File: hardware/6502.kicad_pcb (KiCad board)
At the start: 2 copper layers, 149.9 x 99.1 mm, 80 parts, among them J1 JMP, J10 JMP, J11 Conn_01x04_Male, J12 Conn_01x08_Male, J13 Conn_01x08_Male, J14 Conn_01x06_Male, J15 Conn_01x08_Male, J16 Conn_01x16_Male, J2 Conn_01x16_Male, J3 CA, J4 CB, J5 W27c512?, J6 DB15_Female_HighDensity, J7 Conn_01x12_Male, J8 Barrel_Jack_MountingPin, J9 USB_B_Micro, SW1 SW_Push, U1 74HC00, U10 74HC245, U11 74HC245, U12 PMS171B-SOP16_150mil, U13 74HC245, U14 74HC04, U15 MIC5504-3.3YM5, U16 62256, U17 74LS00, U18 w27C512, U19 74LS161, U2 R6502, U20 74LS165, U3 R6522, U4 74HC273, U5 SST39SF010, U6 74LS161, U7 74LS161, U8 74LS32, U9 74HC245, Y1 16Mhz

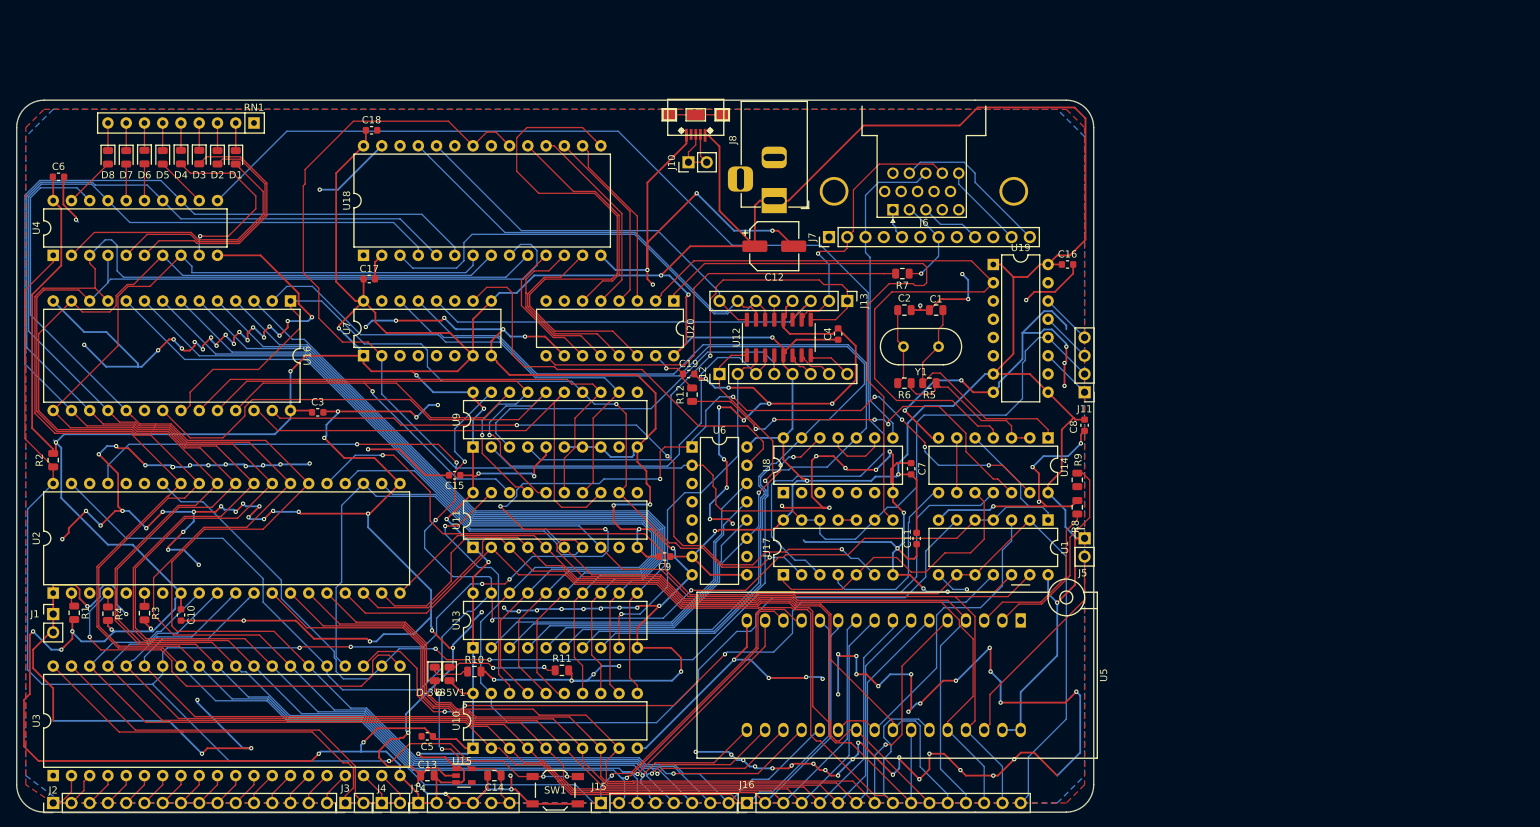
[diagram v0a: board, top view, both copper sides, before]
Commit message: PCB Silkscreen annotations added
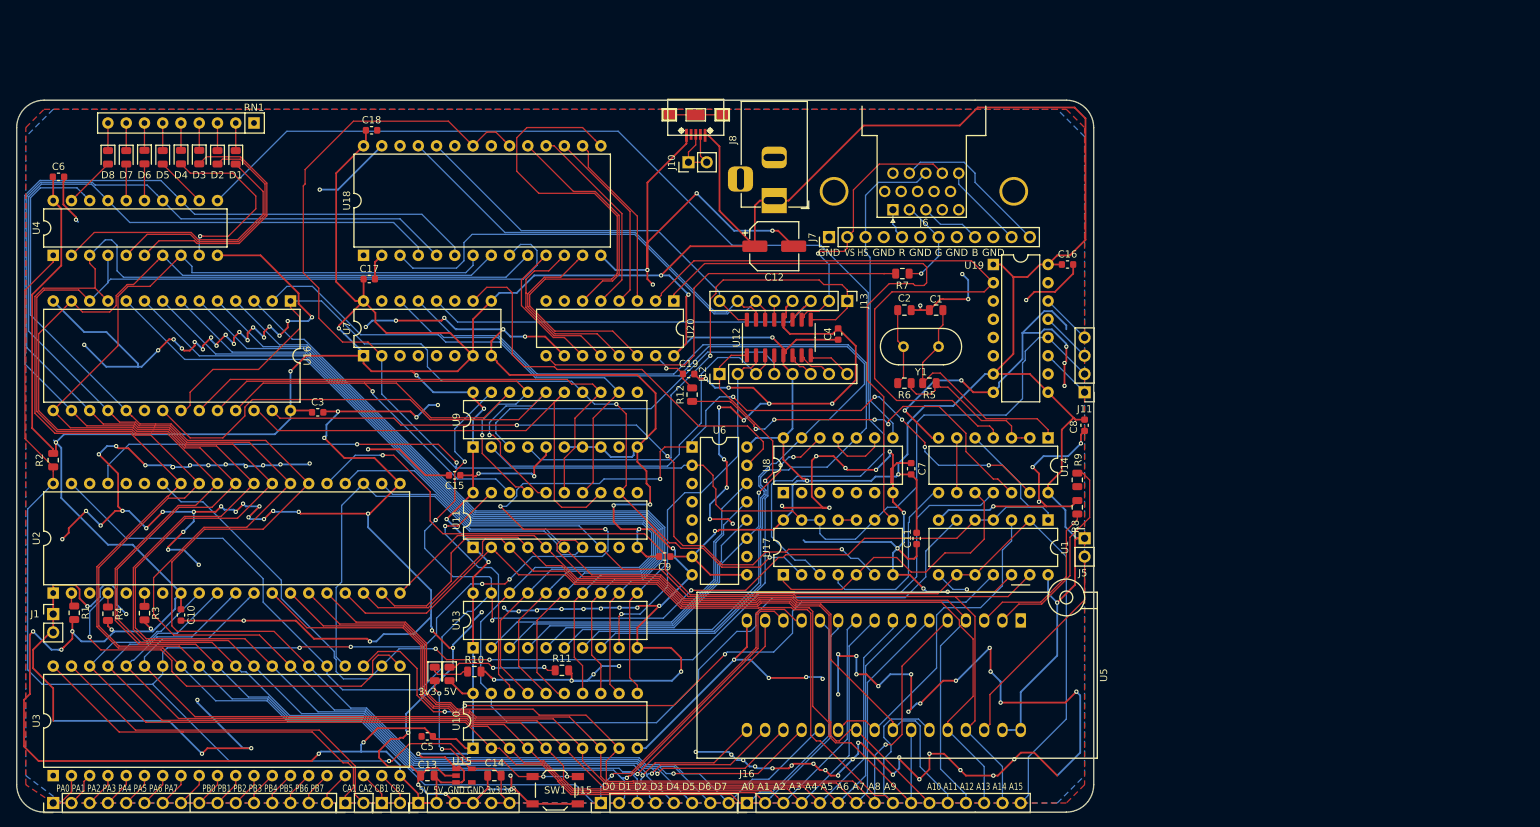
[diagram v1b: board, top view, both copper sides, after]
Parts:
- renumbered D-3v3 to 3v3, D-5V1 to 5V
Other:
- board text added: "5V 5V GND GND 3v3 3v3"
- board text added: "A0 A1 A2 A3 A4 A5 A6 A7 A8 A9"
- board text added: "A10 A11 A12 A13 A14 A15"
- board text added: "B"
- board text added: "CA1 CA2 CB1 CB2"
- board text added: "D0 D1 D2 D3 D4 D5 D6 D7"
- board text added: "G"
- board text added: "GND"
- board text added: "PA0 PA1 PA2 PA3 PA4 PA5 PA6 PA7"
- board text added: "PB0 PB1 PB2 PB3 PB4 PB5 PB6 PB7"
- board text added: "R"
- board text added: "VS HS"

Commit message: Wireless nRF24L01+ bootloader added! No more Padauk PMS171b!
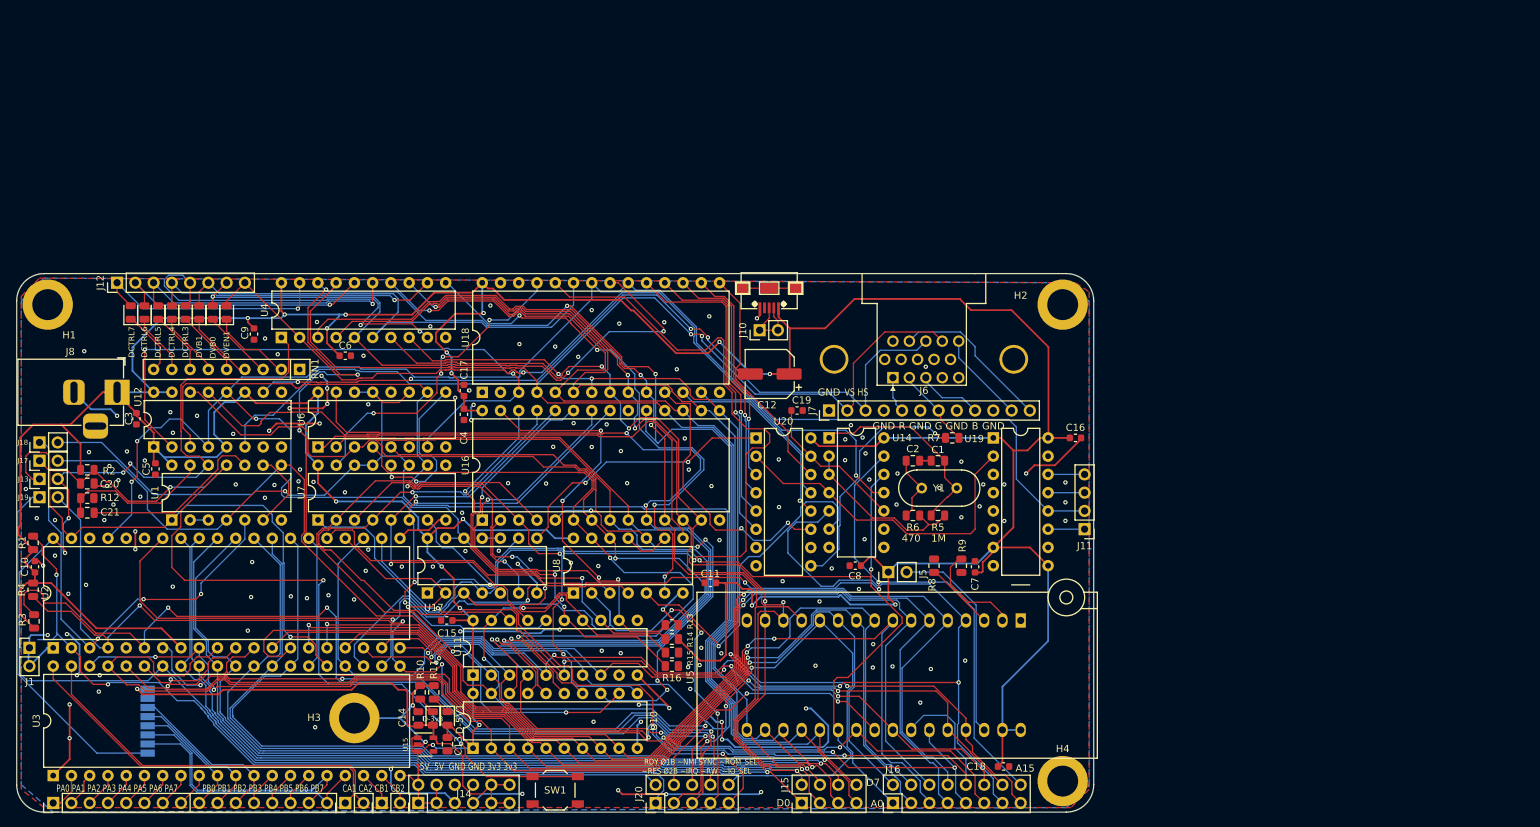
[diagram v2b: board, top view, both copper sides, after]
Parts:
- removed D1, D2, D3, D4, D5, D6, D7, D8: RED, LED_SMD:LED_0805_2012Metric
- removed U13: 74HC245, Package_DIP:DIP-20_W7.62mm
- added C20: 1uF, Capacitor_SMD:C_0805_2012Metric, F.Cu at (22.5, 120.7)
- added C21: 1uF, Capacitor_SMD:C_0805_2012Metric, F.Cu at (22.5, 124.7)
- added DCTRL3: RED, LED_SMD:LED_0805_2012Metric, F.Cu at (36.2, 96.9)
- added DCTRL4: RED, LED_SMD:LED_0805_2012Metric, F.Cu at (34.3, 96.9)
- added DCTRL5: RED, LED_SMD:LED_0805_2012Metric, F.Cu at (32.4, 96.9)
- added DCTRL6: RED, LED_SMD:LED_0805_2012Metric, F.Cu at (30.5, 96.9)
- added DCTRL7: RED, LED_SMD:LED_0805_2012Metric, F.Cu at (28.6, 96.9)
- added DVB0: RED, LED_SMD:LED_0805_2012Metric, F.Cu at (40.0, 96.9)
- added DVB1: RED, LED_SMD:LED_0805_2012Metric, F.Cu at (38.1, 96.9)
- added DVEN1: RED, LED_SMD:LED_0805_2012Metric, F.Cu at (41.9, 96.9)
- added H1: MountingHole_Pad, MountingHole:MountingHole_4.3mm_M4_ISO14580_Pad, F.Cu at (17.0, 95.8)
- added H2: MountingHole_Pad, MountingHole:MountingHole_4.3mm_M4_ISO14580_Pad, F.Cu at (158.2, 95.8)
- added H3: MountingHole_Pad, MountingHole:MountingHole_4.3mm_M4_ISO14580_Pad, F.Cu at (59.7, 153.3)
- added H4: MountingHole_Pad, MountingHole:MountingHole_4.3mm_M4_ISO14580_Pad, F.Cu at (158.2, 162.1)
- added J17: JMP, Connector_PinHeader_2.54mm:PinHeader_1x02_P2.54mm_Vertical, F.Cu at (15.9, 117.5)
- added J18: JMP, Connector_PinHeader_2.54mm:PinHeader_1x02_P2.54mm_Vertical, F.Cu at (15.9, 114.9)
- added J19: JMP, Connector_PinHeader_2.54mm:PinHeader_1x02_P2.54mm_Vertical, F.Cu at (15.9, 122.6)
- added J20: Interface, Connector_PinHeader_2.54mm:PinHeader_2x05_P2.54mm_Vertical, F.Cu at (101.6, 165.1)
- added R13: 2k2, Resistor_SMD:R_0805_2012Metric, F.Cu at (103.9, 140.3)
- added R14: 2k2, Resistor_SMD:R_0805_2012Metric, F.Cu at (103.9, 142.3)
- added R15: 2k2, Resistor_SMD:R_0805_2012Metric, F.Cu at (103.9, 144.2)
- added R16: 2k2, Resistor_SMD:R_0805_2012Metric, F.Cu at (103.9, 146.1)
- J12: value Conn_01x08_Male -> Control_bus
- J13: value Conn_01x08_Male -> EzRST; footprint Connector_PinHeader_2.54mm:PinHeader_1x08_P2.54mm_Vertical -> Connector_PinHeader_2.54mm:PinHeader_1x02_P2.54mm_Vertical
- J14: value Conn_01x06_Male -> Power; footprint Connector_PinHeader_2.54mm:PinHeader_1x06_P2.54mm_Vertical -> Connector_PinHeader_2.54mm:PinHeader_2x06_P2.54mm_Vertical
- J15: value Conn_01x08_Male -> Data_bus; footprint Connector_PinHeader_2.54mm:PinHeader_1x08_P2.54mm_Vertical -> Connector_PinHeader_2.54mm:PinHeader_2x04_P2.54mm_Vertical
- J16: value Conn_01x16_Male -> Address bus; footprint Connector_PinHeader_2.54mm:PinHeader_1x16_P2.54mm_Vertical -> Connector_PinHeader_2.54mm:PinHeader_2x08_P2.54mm_Vertical
- J2: value Conn_01x16_Male -> PORTAB
- R12: value R_Pull -> 150k
- R7: value 150 -> 300
- U1: value 74HC00 -> 74HC14
- U12: value PMS171B-SOP16_150mil -> 74HC109; footprint Package_SO:SOIC-16_3.9x9.9mm_P1.27mm -> Package_DIP:DIP-16_W7.62mm
- U17: value 74LS00 -> 74HC00
- U6, U7: value 74LS161 -> 74HC590
- U8: value 74LS32 -> 74HC32
- U9: value 74HC245 -> NRF24L01_Breakout; footprint Package_DIP:DIP-20_W7.62mm -> mysensors_radios:NRF24L01-SMD; moved to B.Cu
- moved C18 124.8 mm to (150.0, 160.0)
- moved U1 121.9 mm to (34.3, 125.7), turned to 90 degrees
- moved J13 115.1 mm to (15.9, 120.0), turned to 90 degrees
- moved J8 95.2 mm to (26.7, 108.0), turned to 0 degrees
- moved U12 88.3 mm to (31.8, 115.6)
- moved R12 85.4 mm to (22.5, 122.7), turned to 0 degrees
- moved J12 84.8 mm to (26.7, 92.7)
- moved U9 66.1 mm to (22.2, 153.7), turned to -90 degrees
- moved C9 65.0 mm to (45.7, 99.8), turned to -90 degrees
- moved C4 53.3 mm to (74.9, 111.0), turned to -90 degrees
- moved C5 53.1 mm to (32.0, 118.6), turned to -90 degrees
- moved U6 52.1 mm to (54.6, 115.6), turned to 90 degrees
- moved U17 49.6 mm to (69.8, 135.9)
- moved C6 47.0 mm to (58.4, 102.9)
- moved U16 40.5 mm to (77.5, 125.7), turned to 90 degrees
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- renumbered 3v3 to D-3v3, 5V to D-5V1
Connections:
- net Net-(R1-Pad2) renamed RDY
- net Net-(R3-Pad2) renamed ~{NMI}
- net Net-(R4-Pad2) renamed ~{IRQ}
- J12 pad 1: C11 -> Net-(DCTRL7-Pad2)
- J12 pad 2: C12 -> Net-(DCTRL6-Pad2)
- J12 pad 3: C13 -> Net-(DCTRL5-Pad2)
- J12 pad 4: C14 -> Net-(DCTRL4-Pad2)
- J12 pad 5: +5V -> Net-(DCTRL3-Pad2)
- J12 pad 6: VBLANK -> VB1
- J12 pad 7: Net-(J12-Pad7) -> VB0
- J12 pad 8: Net-(J12-Pad8) -> VEN
- J13 pad 1: C15 -> Net-(C20-Pad1)
- J13 pad 2: VSYNC -> ~{RES}
- J14 pad 3: GND -> +5V
- J14 pad 4: GND -> +5V
- J14 pad 5: +3V3 -> GND
- J14 pad 6: +3V3 -> GND
- J2 pad 10: Net-(J2-Pad10) -> RF_CS
- J2 pad 11: Net-(J2-Pad11) -> RF_CE
- J2 pad 15: Net-(J2-Pad15) -> MOSI
- J2 pad 16: Net-(J2-Pad16) -> MISO
- J2 pad 9: Net-(J2-Pad9) -> SPI_CLK
- J6 pad 11: Net-(J6-Pad11) -> unconnected-(J6-Pad11)
- J6 pad 4: Net-(J6-Pad4) -> unconnected-(J6-Pad4)
- J6 pad 9: Net-(J6-Pad9) -> unconnected-(J6-Pad9)
- J9 pad 4: Net-(J9-Pad4) -> unconnected-(J9-Pad4)
- J9 pad 6: Net-(J9-Pad6) -> unconnected-(J9-Pad6)
- R12 pad 1: RES -> Net-(C21-Pad1)
- R12 pad 2: Net-(C19-Pad1) -> GND
- R2 pad 2: ~RES -> Net-(C20-Pad1)
- SW1 pad 2: ~RES -> Net-(C20-Pad1)
- U1 pad 10: A15 -> Net-(C21-Pad2)
- U1 pad 11: ~IO_SEL -> Net-(C20-Pad1)
- U1 pad 12: Net-(U1-Pad12) -> ~{RES}
- U1 pad 13: A14 -> Net-(C21-Pad1)
- U1 pad 2: A15 -> Net-(U1-Pad2)
- U1 pad 3: ~ROM_SEL -> Net-(U1-Pad2)
- U1 pad 4: Ø2 -> Ø2B
- U1 pad 5: Ø2 -> Ø1
- U1 pad 6: ~RAM_SEL -> Net-(U1-Pad6)
- U1 pad 8: Net-(U1-Pad12) -> Ø1B
- U1 pad 9: A15 -> Net-(U1-Pad6)
- U10 pad 11: Net-(U10-Pad11) -> C11
- U10 pad 12: Net-(U10-Pad12) -> C10
- U10 pad 13: Net-(U10-Pad13) -> C5
- U10 pad 14: Net-(U10-Pad14) -> C4
- U10 pad 15: Net-(U10-Pad15) -> C3
- U10 pad 16: Net-(U10-Pad16) -> C2
- U10 pad 17: Net-(U10-Pad17) -> C1
- U10 pad 18: Net-(U10-Pad18) -> C0
- U10 pad 19: ~RAM_SEL -> Ø1B
- U11 pad 11: Net-(U11-Pad11) -> unconnected-(U11-Pad11)
- U11 pad 12: Net-(U11-Pad12) -> Net-(R13-Pad2)
- U11 pad 13: Net-(U11-Pad13) -> Net-(R14-Pad2)
- U11 pad 14: Net-(U11-Pad14) -> Net-(R15-Pad2)
- U11 pad 15: Net-(U11-Pad15) -> Net-(R16-Pad2)
- U11 pad 16: Net-(U11-Pad16) -> C14
- U11 pad 17: Net-(U11-Pad17) -> C13
- U11 pad 18: Net-(U11-Pad18) -> C12
- U11 pad 19: ~RAM_SEL -> Ø1B
- U11 pad 9: Net-(U11-Pad9) -> unconnected-(U11-Pad9)
- U12 pad 1: C11 -> +5V
- U12 pad 10: VSYNC -> HSYNC
- U12 pad 11: C6 -> +5V
- U12 pad 12: GND -> 2Mhz
- U12 pad 13: C7 -> Net-(U12-Pad13)
- U12 pad 14: C8 -> C3
- U12 pad 15: C9 -> +5V
- U12 pad 16: C10 -> +5V
- U12 pad 2: C12 -> C7
- U12 pad 3: C13 -> ~{VCRST}
- U12 pad 4: C14 -> 2Mhz
- U12 pad 6: VBLANK -> VSYNC
- U12 pad 7: Net-(J12-Pad7) -> unconnected-(U12-Pad7)
- U12 pad 8: Net-(J12-Pad8) -> GND
- U12 pad 9: C15 -> unconnected-(U12-Pad9)
- U14 pad 10: Net-(U14-Pad10) -> Net-(C19-Pad1)
- U14 pad 11: ~RW -> VEN
- U14 pad 12: RES -> ~{ROM_SEL}
- U14 pad 13: ~RES -> A15
- U14 pad 5: Ø2 -> A12
- U14 pad 8: Net-(U14-Pad8) -> (no net)
- U14 pad 9: Net-(U14-Pad6) -> (no net)
- U15 pad 4: Net-(U15-Pad4) -> unconnected-(U15-Pad4)
- U16 pad 1: Net-(U11-Pad12) -> Net-(R13-Pad2)
- U16 pad 10: Net-(U10-Pad18) -> C0
- U16 pad 2: Net-(U11-Pad14) -> Net-(R15-Pad2)
- U16 pad 21: Net-(U11-Pad16) -> C14
- U16 pad 22: Net-(U11-Pad12) -> Net-(R13-Pad2)
- U16 pad 23: Net-(U11-Pad15) -> Net-(R16-Pad2)
- U16 pad 24: Net-(U11-Pad17) -> C13
- U16 pad 25: Net-(U11-Pad18) -> C12
- U16 pad 26: Net-(U11-Pad13) -> Net-(R14-Pad2)
- U16 pad 3: Net-(U10-Pad11) -> C11
- U16 pad 4: Net-(U10-Pad12) -> C10
- U16 pad 5: Net-(U10-Pad13) -> C5
- U16 pad 6: Net-(U10-Pad14) -> C4
- U16 pad 7: Net-(U10-Pad15) -> C3
- U16 pad 8: Net-(U10-Pad16) -> C2
- U16 pad 9: Net-(U10-Pad17) -> C1
- U17 pad 1: Net-(U14-Pad10) -> ~{ROM_SEL}
- U17 pad 2: Net-(U11-Pad12) -> A14
- U17 pad 3: ~LDOUTPUT -> ~{IO_SEL}
- U17 pad 4: Net-(U14-Pad8) -> C9
- U17 pad 5: Net-(U14-Pad10) -> C15
- U17 pad 6: Net-(U16-Pad27) -> ~{VCRST}
- U18 pad 21: GND -> VB0
- U18 pad 23: GND -> VB1
- U18 pad 24: C10 -> C9
- U18 pad 25: C9 -> C8
- U18 pad 3: C8 -> C7
- U19 pad 10: Net-(U19-Pad10) -> unconnected-(U19-Pad10)
- U19 pad 15: Net-(U19-Pad15) -> unconnected-(U19-Pad15)
- U19 pad 3: Net-(U19-Pad3) -> unconnected-(U19-Pad3)
- U19 pad 4: Net-(U19-Pad4) -> unconnected-(U19-Pad4)
- U19 pad 5: Net-(U19-Pad5) -> unconnected-(U19-Pad5)
- U19 pad 6: Net-(U19-Pad6) -> unconnected-(U19-Pad6)
- U2 pad 3: Net-(U2-Pad3) -> Ø1
- U2 pad 34: ~RW -> ~{RW}
- U2 pad 35: Net-(U2-Pad35) -> unconnected-(U2-Pad35)
- U2 pad 36: Net-(U2-Pad36) -> unconnected-(U2-Pad36)
- U2 pad 38: Net-(U2-Pad38) -> unconnected-(U2-Pad38)
- U2 pad 40: ~RES -> ~{RES}
- U2 pad 5: Net-(U2-Pad5) -> unconnected-(U2-Pad5)
- U2 pad 7: Net-(U2-Pad7) -> SYNC
- U20 pad 7: Net-(U20-Pad7) -> unconnected-(U20-Pad7)
- U3 pad 10: Net-(J2-Pad9) -> SPI_CLK
- U3 pad 11: Net-(J2-Pad10) -> RF_CS
- U3 pad 12: Net-(J2-Pad11) -> RF_CE
- U3 pad 16: Net-(J2-Pad15) -> MOSI
- U3 pad 17: Net-(J2-Pad16) -> MISO
- U3 pad 22: ~RW -> ~{RW}
- U3 pad 23: ~IO_SEL -> ~{IO_SEL}
- U3 pad 34: ~RES -> ~{RES}
- U4 pad 1: ~RES -> ~{RES}
- U4 pad 11: ~LDOUTPUT -> ~{LDCTRL}
- U4 pad 12: Net-(D5-Pad2) -> Net-(DCTRL4-Pad2)
- U4 pad 15: Net-(D6-Pad2) -> Net-(DCTRL5-Pad2)
- U4 pad 16: Net-(D7-Pad2) -> Net-(DCTRL6-Pad2)
- U4 pad 19: Net-(D8-Pad2) -> Net-(DCTRL7-Pad2)
- U4 pad 2: Net-(D1-Pad2) -> VEN
- U4 pad 5: Net-(D2-Pad2) -> VB0
- U4 pad 6: Net-(D3-Pad2) -> VB1
- U4 pad 9: Net-(D4-Pad2) -> Net-(DCTRL3-Pad2)
- U5 pad 1: Net-(U5-Pad1) -> unconnected-(U5-Pad1)
- U5 pad 22: ~ROM_SEL -> ~{ROM_SEL}
- U5 pad 24: ~ROM_SEL -> Ø1B
- U6 pad 1: ~RES -> C1
- U6 pad 10: Net-(U6-Pad10) -> ~{VCRST}
- U6 pad 11: C3 -> Ø2B
- U6 pad 12: C2 -> GND
- U6 pad 13: C1 -> Ø2B
- U6 pad 14: C0 -> Ø2B
- U6 pad 15: Net-(U6-Pad15) -> C0
- U6 pad 2: 2Mhz -> C2
- U6 pad 3: Net-(U6-Pad3) -> C3
- U6 pad 4: Net-(U6-Pad4) -> C4
- U6 pad 5: Net-(U6-Pad5) -> C5
- U6 pad 6: Net-(U6-Pad6) -> unconnected-(U6-Pad6)
- U6 pad 7: +5V -> C7
- U6 pad 9: +5V -> Net-(U6-Pad9)
- U7 pad 1: +5V -> C9
- U7 pad 10: Net-(U6-Pad15) -> ~{VCRST}
- U7 pad 11: Net-(U7-Pad11) -> Ø2B
- U7 pad 12: C6 -> Net-(U6-Pad9)
- U7 pad 13: C5 -> Ø2B
- U7 pad 14: C4 -> Ø2B
- U7 pad 15: Net-(U7-Pad15) -> C8
- U7 pad 2: 2Mhz -> C10
- U7 pad 3: Net-(U7-Pad3) -> C11
- U7 pad 4: Net-(U7-Pad4) -> C12
- U7 pad 5: Net-(U7-Pad5) -> C13
- U7 pad 6: Net-(U7-Pad6) -> C14
- U7 pad 7: +5V -> C15
- U7 pad 9: +5V -> unconnected-(U7-Pad9)
- U8 pad 1: (no net) -> Ø1B
- U8 pad 2: (no net) -> ~{RW}
- U8 pad 3: (no net) -> Net-(U16-Pad27)
- U8 pad 4: (no net) -> ~{IO_SEL}
- U8 pad 5: (no net) -> Net-(U14-Pad6)
- U8 pad 6: (no net) -> ~{LDCTRL}
- U8 pad 8: HSYNC -> Net-(U12-Pad13)
- U9 pad 1: +5V -> GND
- U9 pad 2: C13 -> +3V3
- U9 pad 3: C14 -> RF_CE
- U9 pad 4: C15 -> RF_CS
- U9 pad 5: +5V -> SPI_CLK
- U9 pad 6: GND -> MOSI
- U9 pad 7: GND -> MISO
- U9 pad 8: GND -> Net-(J19-Pad1)
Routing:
- net GND: track 1182.5 -> 210.6 mm, vias 166 -> 154
- net ~RES: track 332.7 -> 0.00 mm, vias 15 -> 0
- net ~{RES}: track 0.00 -> 194.5 mm, vias 0 -> 4
- net +5V: track 846.0 -> 659.2 mm, vias 24 -> 17
- net Ø1B: track 0.00 -> 179.5 mm, vias 0 -> 5
- net Ø2B: track 0.00 -> 176.5 mm, vias 0 -> 2
- net ~LDOUTPUT: track 160.7 -> 0.00 mm
- net Ø2: track 222.6 -> 68.7 mm, vias 4 -> 1
- net ~RW: track 146.6 -> 0.00 mm, vias 2 -> 0
- net ~{RW}: track 0.00 -> 139.9 mm, vias 0 -> 4
- net Net-(C20-Pad1): track 0.00 -> 135.2 mm, vias 0 -> 3
- net ~{ROM_SEL}: track 0.00 -> 135.1 mm, vias 0 -> 2
- net ~{NMI}: track 1.86 -> 128.7 mm, vias 0 -> 3
- net Net-(U10-Pad18): track 126.8 -> 0.00 mm
- net Net-(U10-Pad17): track 124.2 -> 0.00 mm
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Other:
- board size 149.9 x 99.1 mm -> 149.9 x 74.9 mm
- net class Default removed
- net class Power removed
- rule pad_to_mask_clearance: 0.051 -> 0
- board text added: "A0"
- board text added: "A15"
- board text added: "D0"
- board text added: "D7"
- board text added: "RDY Ø1B ~NMI SYNC ~ROM_SEL ~RES Ø2B ~IRQ ~RW ~IO_SEL"
- board text removed: "A0 A1 A2 A3 A4 A5 A6 A7 A8 A9"
- board text removed: "A10 A11 A12 A13 A14 A15"
- board text removed: "D0 D1 D2 D3 D4 D5 D6 D7"

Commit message: R1B2 gerbers, start+stop bits in modem driver
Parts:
- removed J13: EzRST, Connector_PinHeader_2.54mm:PinHeader_1x02_P2.54mm_Vertical
- removed J18, J19: JMP, Connector_PinHeader_2.54mm:PinHeader_1x02_P2.54mm_Vertical
- added C22: 10uF, Capacitor_SMD:C_0805_2012Metric, F.Cu at (86.2, 61.1)
- added C23: 100nF, Capacitor_SMD:C_0603_1608Metric, F.Cu at (216.4, 74.6)
- added C24: 100nF, Capacitor_SMD:C_0603_1608Metric, F.Cu at (180.8, 65.0)
- added C25: 100nF, Capacitor_SMD:C_0603_1608Metric, F.Cu at (78.2, 79.8)
- added R17: NC, Resistor_SMD:R_0805_2012Metric, B.Cu at (148.1, 84.3)
- added R18: 2k2, Resistor_SMD:R_0805_2012Metric, B.Cu at (155.2, 84.3)
- added R19: NC, Resistor_SMD:R_0805_2012Metric, B.Cu at (157.2, 84.3)
- added R20: NC, Resistor_SMD:R_0805_2012Metric, B.Cu at (159.3, 84.3)
- added R21: NC, Resistor_SMD:R_0805_2012Metric, B.Cu at (161.3, 84.3)
- added R22: 2k2, Resistor_SMD:R_0805_2012Metric, B.Cu at (164.5, 96.9)
- added R23: NC, Resistor_SMD:R_0805_2012Metric, B.Cu at (142.0, 84.3)
- added R24: NC, Resistor_SMD:R_0805_2012Metric, B.Cu at (144.0, 84.3)
- added R25: NC, Resistor_SMD:R_0805_2012Metric, B.Cu at (146.1, 84.3)
- added R26: 0R, Resistor_SMD:R_0402_1005Metric, B.Cu at (141.7, 87.0)
- added R27: NC, Resistor_SMD:R_0402_1005Metric, B.Cu at (141.7, 88.0)
- added R28: 0R, Resistor_SMD:R_0402_1005Metric_Pad0.72x0.64mm_HandSolder, F.Cu at (74.9, 107.1)
- added R29: NC, Resistor_SMD:R_0402_1005Metric_Pad0.72x0.64mm_HandSolder, B.Cu at (83.5, 104.7)
- added R30: NC, Resistor_SMD:R_0402_1005Metric_Pad0.72x0.64mm_HandSolder, F.Cu at (217.7, 69.3)
- added R31: NC, Resistor_SMD:R_0402_1005Metric, B.Cu at (143.7, 119.0)
- added R32: NC, Resistor_SMD:R_0402_1005Metric, B.Cu at (144.6, 119.0)
- added R33: NC, Resistor_SMD:R_0402_1005Metric, B.Cu at (145.6, 119.0)
- added R34: NC, Resistor_SMD:R_0402_1005Metric, B.Cu at (146.5, 119.0)
- added R35: NC, Resistor_SMD:R_0402_1005Metric, B.Cu at (147.4, 119.0)
- added R36: NC, Resistor_SMD:R_0402_1005Metric, B.Cu at (148.4, 119.0)
- added R37: NC, Resistor_SMD:R_0402_1005Metric, B.Cu at (149.3, 119.0)
- added R38: NC, Resistor_SMD:R_0402_1005Metric, B.Cu at (150.3, 119.0)
- added R39: NC, Resistor_SMD:R_0402_1005Metric, B.Cu at (138.3, 109.4)
- added R40: NC, Resistor_SMD:R_0402_1005Metric, B.Cu at (140.5, 109.3)
- added R41: NC, Resistor_SMD:R_0402_1005Metric, B.Cu at (143.1, 109.7)
- added R42: NC, Resistor_SMD:R_0402_1005Metric, B.Cu at (145.2, 109.4)
- added R43: NC, Resistor_SMD:R_0402_1005Metric, B.Cu at (147.5, 109.4)
- added R44: NC, Resistor_SMD:R_0402_1005Metric, B.Cu at (151.0, 109.4)
- added R45: NC, Resistor_SMD:R_0402_1005Metric, B.Cu at (153.5, 109.4)
- added R46: NC, Resistor_SMD:R_0402_1005Metric, B.Cu at (156.1, 109.4)
- added R47: NC, Resistor_SMD:R_0402_1005Metric_Pad0.72x0.64mm_HandSolder, B.Cu at (86.2, 94.3)
- added R48: 0R, Resistor_SMD:R_0805_2012Metric, B.Cu at (110.3, 118.0)
- added R49: NC, Resistor_SMD:R_0805_2012Metric, B.Cu at (107.1, 118.0)
- added U13: 74HC74, Package_DIP:DIP-14_W7.62mm, F.Cu at (200.4, 78.5)
- added U21: 74HC00, Package_DIP:DIP-14_W7.62mm, F.Cu at (73.9, 89.9)
- C20, C21, R12, R13, R14, R15, R2, R7: moved to B.Cu
- J1: value JMP -> 5V
- J11: value Conn_01x04_Male -> GPCO; footprint Connector_PinHeader_2.54mm:PinHeader_1x04_P2.54mm_Vertical -> Connector_PinHeader_2.54mm:PinHeader_1x05_P2.54mm_Vertical
- J17: value JMP -> USB_A; footprint Connector_PinHeader_2.54mm:PinHeader_1x02_P2.54mm_Vertical -> Connector_USB:USB_A_Molex_67643_Horizontal
- J8: value Barrel_Jack_MountingPin -> 5V; footprint Connector_BarrelJack:BarrelJack_Horizontal -> Connector_PinHeader_2.54mm:PinHeader_1x02_P2.54mm_Vertical
- R16: value 2k2 -> NC; moved to B.Cu
- moved J8 197.8 mm to (220.7, 69.8)
- moved J1 108.8 mm to (83.6, 59.5), turned to 180 degrees
- moved C21 90.2 mm to (104.1, 86.3), turned to 90 degrees
- moved R12 87.5 mm to (102.1, 86.3), turned to 90 degrees
- moved J17 85.5 mm to (85.1, 67.3), turned to -90 degrees
- moved C20 84.8 mm to (100.0, 86.3), turned to 90 degrees
- moved R2 82.1 mm to (97.9, 86.3), turned to 90 degrees
- moved R13 73.1 mm to (162.6, 96.9), turned to -90 degrees
- moved R14 72.7 mm to (160.7, 96.9), turned to -90 degrees
- moved R15 72.5 mm to (158.8, 96.9), turned to -90 degrees
- moved R16 72.3 mm to (156.9, 96.9), turned to -90 degrees
- moved C16 72.1 mm to (220.5, 74.9)
- moved R8 71.6 mm to (202.9, 97.3)
- moved U19 71.6 mm to (210.6, 78.5)
- moved C2 71.0 mm to (196.1, 77.6)
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- renumbered D-3v3 to 3v3, D-5V1 to 5V0
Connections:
- net Net-(DCTRL3-Pad2) renamed CTRL3
- net Net-(DCTRL4-Pad2) renamed CTRL4
- net Net-(DCTRL5-Pad2) renamed CTRL5
- net Net-(DCTRL6-Pad2) renamed CTRL6
- net Net-(DCTRL7-Pad2) renamed CTRL7
- net Net-(J4-Pad1) renamed CB1
- net ~{LDCTRL} renamed Net-(U4-Pad11)
- J1 pad 1: GND -> +5V
- J17 pad 1: Ø2 -> +5V
- J17 pad 2: Ø2B -> CB2
- J2 pad 12: Net-(J2-Pad12) -> SDA_VGA
- J2 pad 14: Net-(J2-Pad14) -> MISO
- J2 pad 15: MOSI -> PB6
- J2 pad 16: MISO -> MOSI
- J20 pad 3: Ø2B -> 2Mhz
- J4 pad 2: Net-(J4-Pad2) -> CB2
- J6 pad 9: unconnected-(J6-Pad9) -> Net-(J6-Pad9)
- R14 pad 1: +5V -> GND
- U1 pad 1: Ø2 -> ~{RW}
- U1 pad 3: Net-(U1-Pad2) -> A12
- U1 pad 4: Ø2B -> Net-(U1-Pad4)
- U1 pad 5: Ø1 -> Net-(U1-Pad5)
- U1 pad 6: Net-(U1-Pad6) -> VIACS1
- U1 pad 8: Ø1B -> Net-(U1-Pad8)
- U1 pad 9: Net-(U1-Pad6) -> Net-(U1-Pad9)
- U11 pad 11: unconnected-(U11-Pad11) -> Net-(R22-Pad2)
- U11 pad 9: unconnected-(U11-Pad9) -> A15
- U14 pad 5: A12 -> Net-(U14-Pad5)
- U14 pad 8: (no net) -> unconnected-(U14-Pad8)
- U14 pad 9: (no net) -> GND
- U16 pad 20: GND -> Net-(R22-Pad2)
- U16 pad 22: Net-(R13-Pad2) -> Net-(U14-Pad6)
- U17 pad 10: Net-(U17-Pad10) -> Ø1B
- U17 pad 11: Net-(U17-Pad10) -> Ø1B
- U18 pad 2: GND -> VB1
- U18 pad 21: VB0 -> C9
- U18 pad 23: VB1 -> VB0
- U18 pad 24: C9 -> C8
- U18 pad 25: C8 -> C7
- U18 pad 3: C7 -> D7
- U2 pad 1: GND -> Net-(R28-Pad1)
- U2 pad 36: unconnected-(U2-Pad36) -> Net-(R47-Pad2)
- U3 pad 13: Net-(J2-Pad12) -> SDA_VGA
- U3 pad 15: Net-(J2-Pad14) -> MISO
- U3 pad 16: MOSI -> PB6
- U3 pad 17: MISO -> MOSI
- U3 pad 19: Net-(J4-Pad2) -> CB2
- U3 pad 24: A13 -> VIACS1
- U6 pad 11: Ø2B -> 2Mhz
- U6 pad 13: Ø2B -> 2Mhz
- U6 pad 14: Ø2B -> 2Mhz
- U7 pad 11: Ø2B -> 2Mhz
- U7 pad 13: Ø2B -> 2Mhz
- U7 pad 14: Ø2B -> 2Mhz
- U8 pad 5: Net-(U14-Pad6) -> Net-(U21-Pad6)
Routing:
- net PB6: track 0.00 -> 229.0 mm, vias 0 -> 5
- net Ø2B: track 176.5 -> 0.00 mm, vias 2 -> 0
- net SDA_VGA: track 22.6 -> 192.8 mm, vias 0 -> 4
- net SCL_VGA: track 12.7 -> 176.7 mm, vias 0 -> 3
- net 2Mhz: track 245.8 -> 397.5 mm, vias 3 -> 2
- net CB1: track 4.86 -> 150.3 mm, vias 0 -> 8
- net Net-(U14-Pad5): track 0.00 -> 109.1 mm, vias 0 -> 3
- net Net-(R13-Pad2): track 63.3 -> 170.0 mm, vias 2 -> 5
- net CB2: track 0.00 -> 106.5 mm, vias 0 -> 3
- net Net-(U21-Pad6): track 0.00 -> 87.6 mm, vias 0 -> 4
- net Net-(R26-Pad1): track 0.00 -> 69.6 mm, vias 0 -> 2
- net Ø1B: track 179.5 -> 112.5 mm
- net Ø1: track 63.3 -> 0.00 mm, vias 3 -> 0
- net CTRL5: track 38.3 -> 101.3 mm, vias 1 -> 5
- net Net-(R22-Pad2): track 0.00 -> 60.2 mm, vias 0 -> 3
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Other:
- board text added: "ABNielsen.com 6502 SBC r1 b2"
- board text added: "SCL"
- board text added: "SDA"
- board text removed: "ABNielsen.com 6502 SBC r1"
